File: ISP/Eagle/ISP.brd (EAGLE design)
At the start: 57.1 x 55.5 mm, 28 parts, among them IC1 FT232RL, IC2 ATMEGA328P-AU, Q1 16MHz, T1 BC847, U1 IP4220CZ6, X2 MINI-USB_SHIELD4P-85-32004-00X

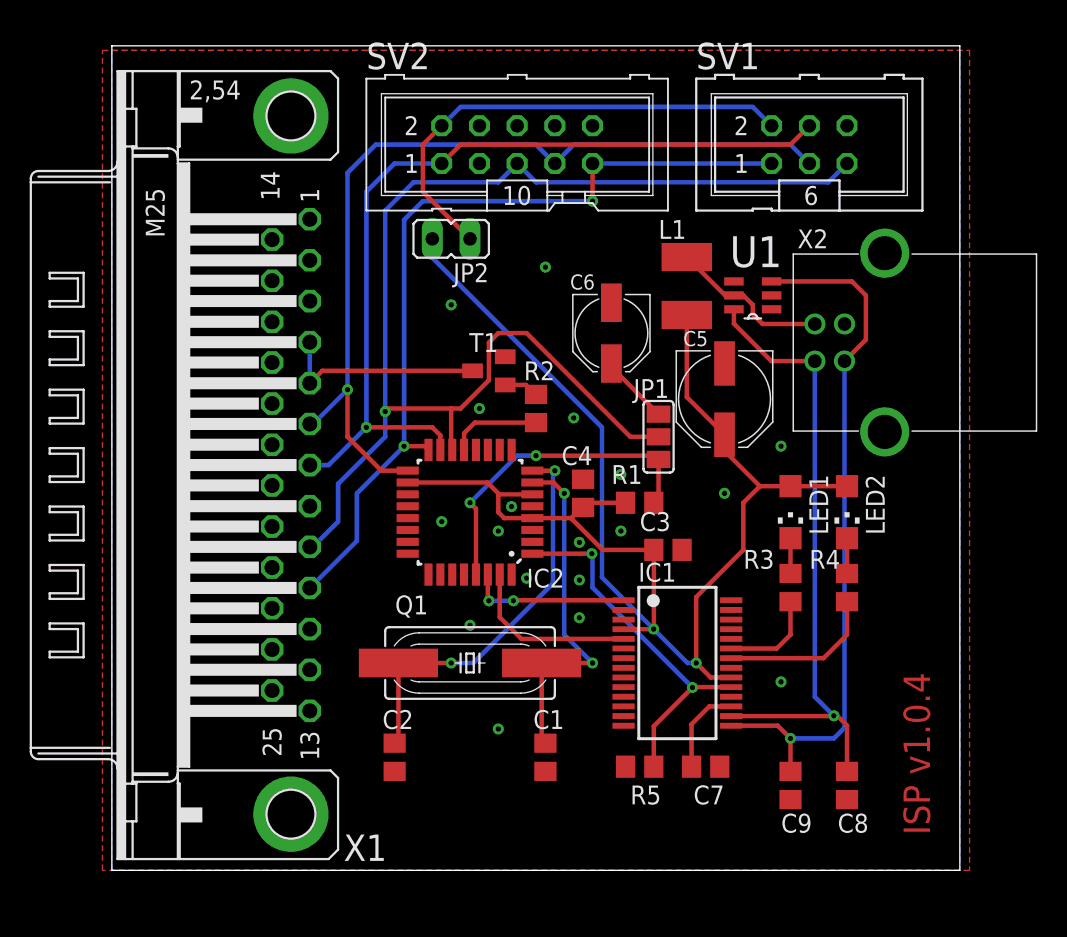
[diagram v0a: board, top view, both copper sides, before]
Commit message: Shorten the Curcit Board
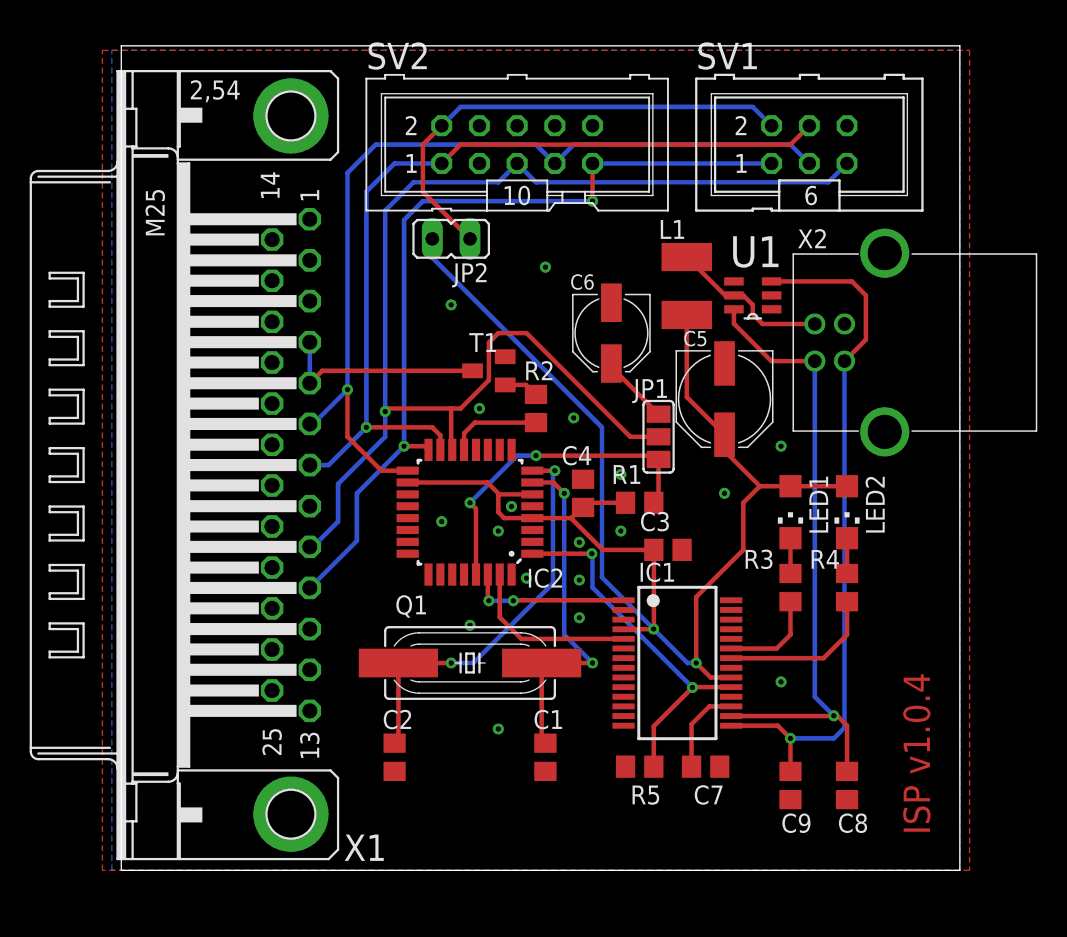
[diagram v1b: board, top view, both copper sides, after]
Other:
- board size 57.1 x 55.5 mm -> 56.5 x 55.5 mm
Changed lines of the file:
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@@
 <?xml version="1.0" encoding="utf-8"?>
 <!DOCTYPE eagle SYSTEM "eagle.dtd">
-<eagle version="9.5.1">
+<eagle version="9.6.2">
 <drawing>
 <settings>
@@
 <board>
 <plain>
-<wire x1="0" y1="0" x2="57.13" y2="0" width="0" layer="20"/>
+<wire x1="0.635" y1="0" x2="57.13" y2="0" width="0" layer="20"/>
 <wire x1="57.13" y1="0" x2="57.13" y2="55.55" width="0" layer="20"/>
-<wire x1="57.13" y1="55.55" x2="0" y2="55.55" width="0" layer="20"/>
-<wire x1="0" y1="55.55" x2="0" y2="0" width="0" layer="20"/>
+<wire x1="57.13" y1="55.55" x2="0.635" y2="55.55" width="0" layer="20"/>
+<wire x1="0.635" y1="55.55" x2="0.635" y2="0" width="0" layer="20"/>
 <text x="53.34" y="13.335" size="1.778" layer="1" rot="R270">ISP v1.0.4</text>
 </plain>
